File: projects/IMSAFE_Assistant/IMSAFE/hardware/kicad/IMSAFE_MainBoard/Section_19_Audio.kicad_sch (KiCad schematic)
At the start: 0 parts

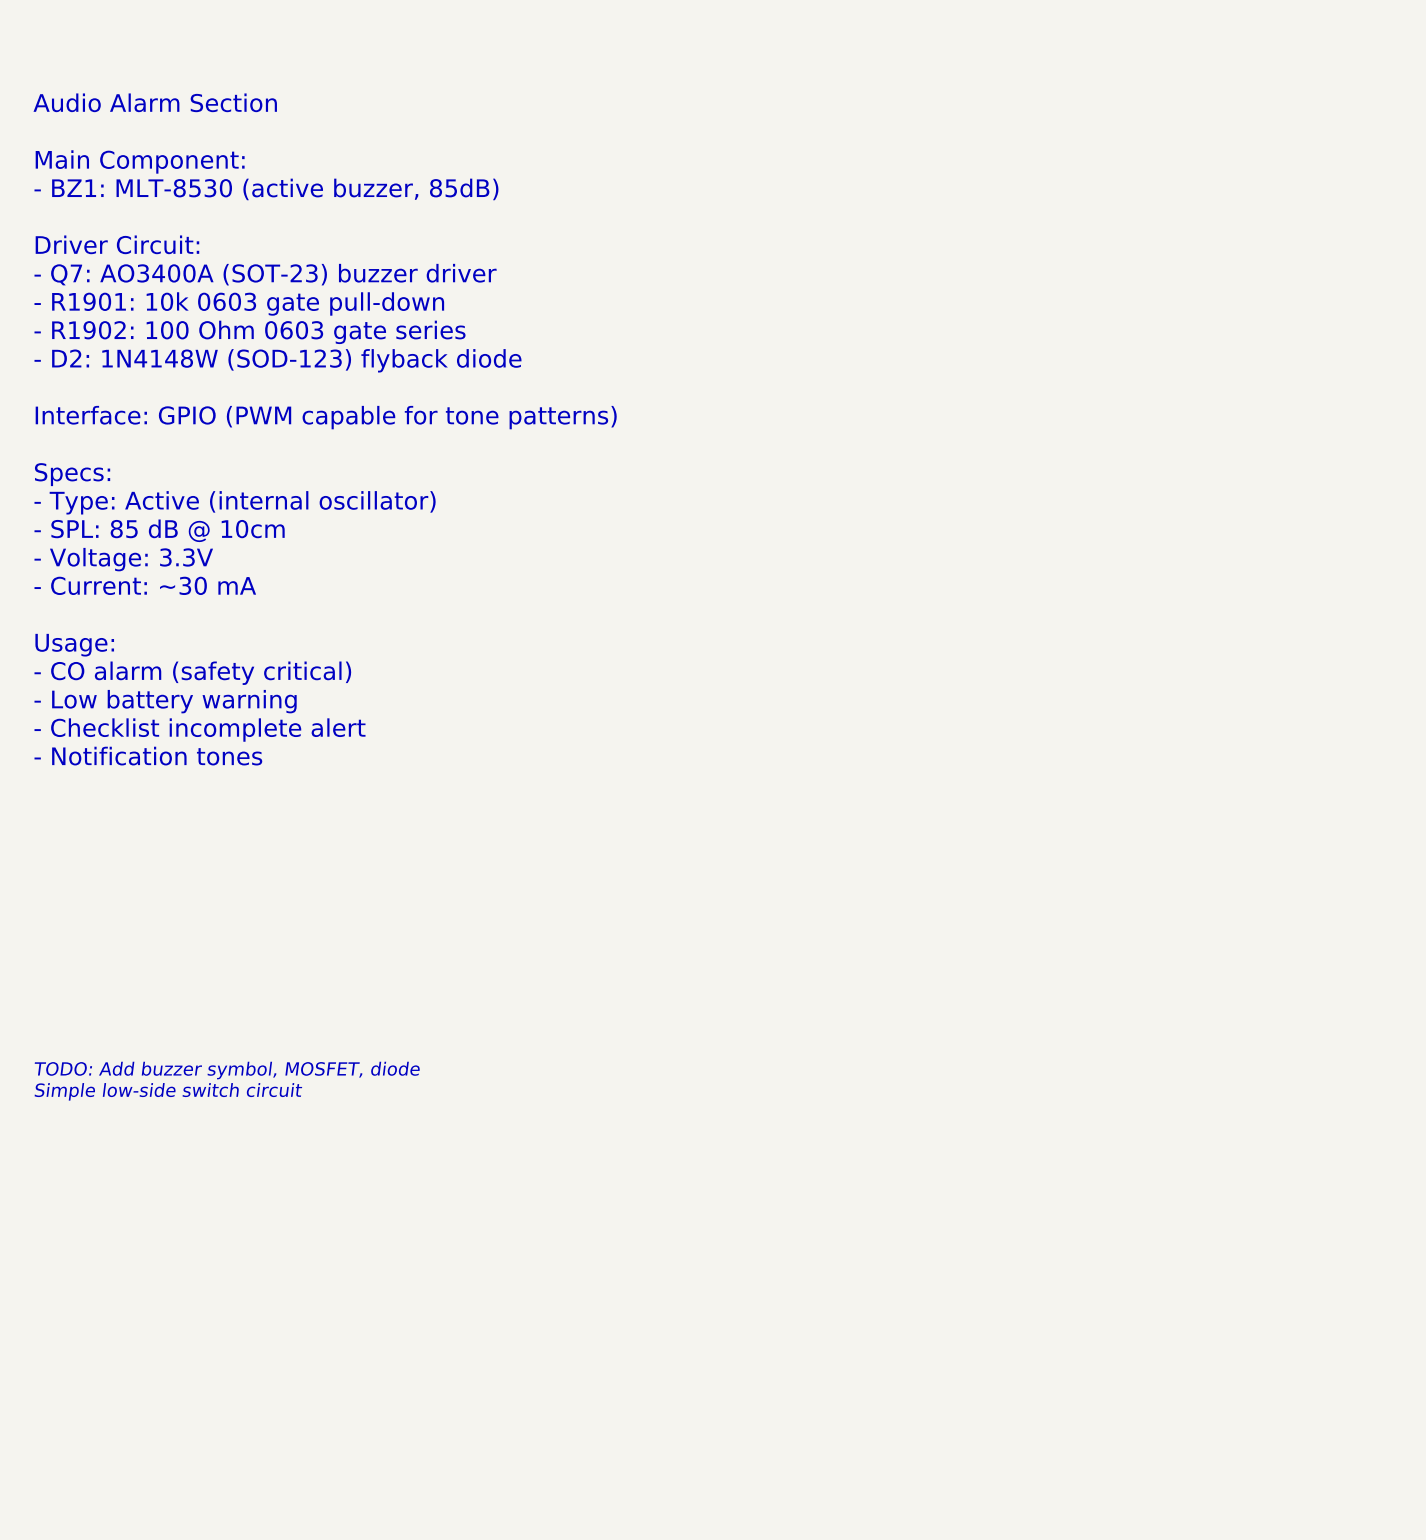
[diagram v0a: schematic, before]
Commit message: Add sensor and interface schematic implementations
- Section 01: MCU Core additional connections
- Section 04: BMS refinements
- Section 07: Barometric sensor (BMP390)
- Section 08: IMU (ICM-42688-P) full implementation
- Section 09: Magnetometer (MMC5983MA) full implementation
- Section 10: Gas sensor (MICS-4514) with heater control
- Section 11: Temp/Humidity (Si7021-A20) implementation
- Section 14: I/O Expander updates
- Section 16: Rotary encoder connections
- Section 19: Audio buzzer (MLT-8530) with MOSFET driver

Co-Authored-By: Claude Opus 4.5 <noreply@anthropic.com>
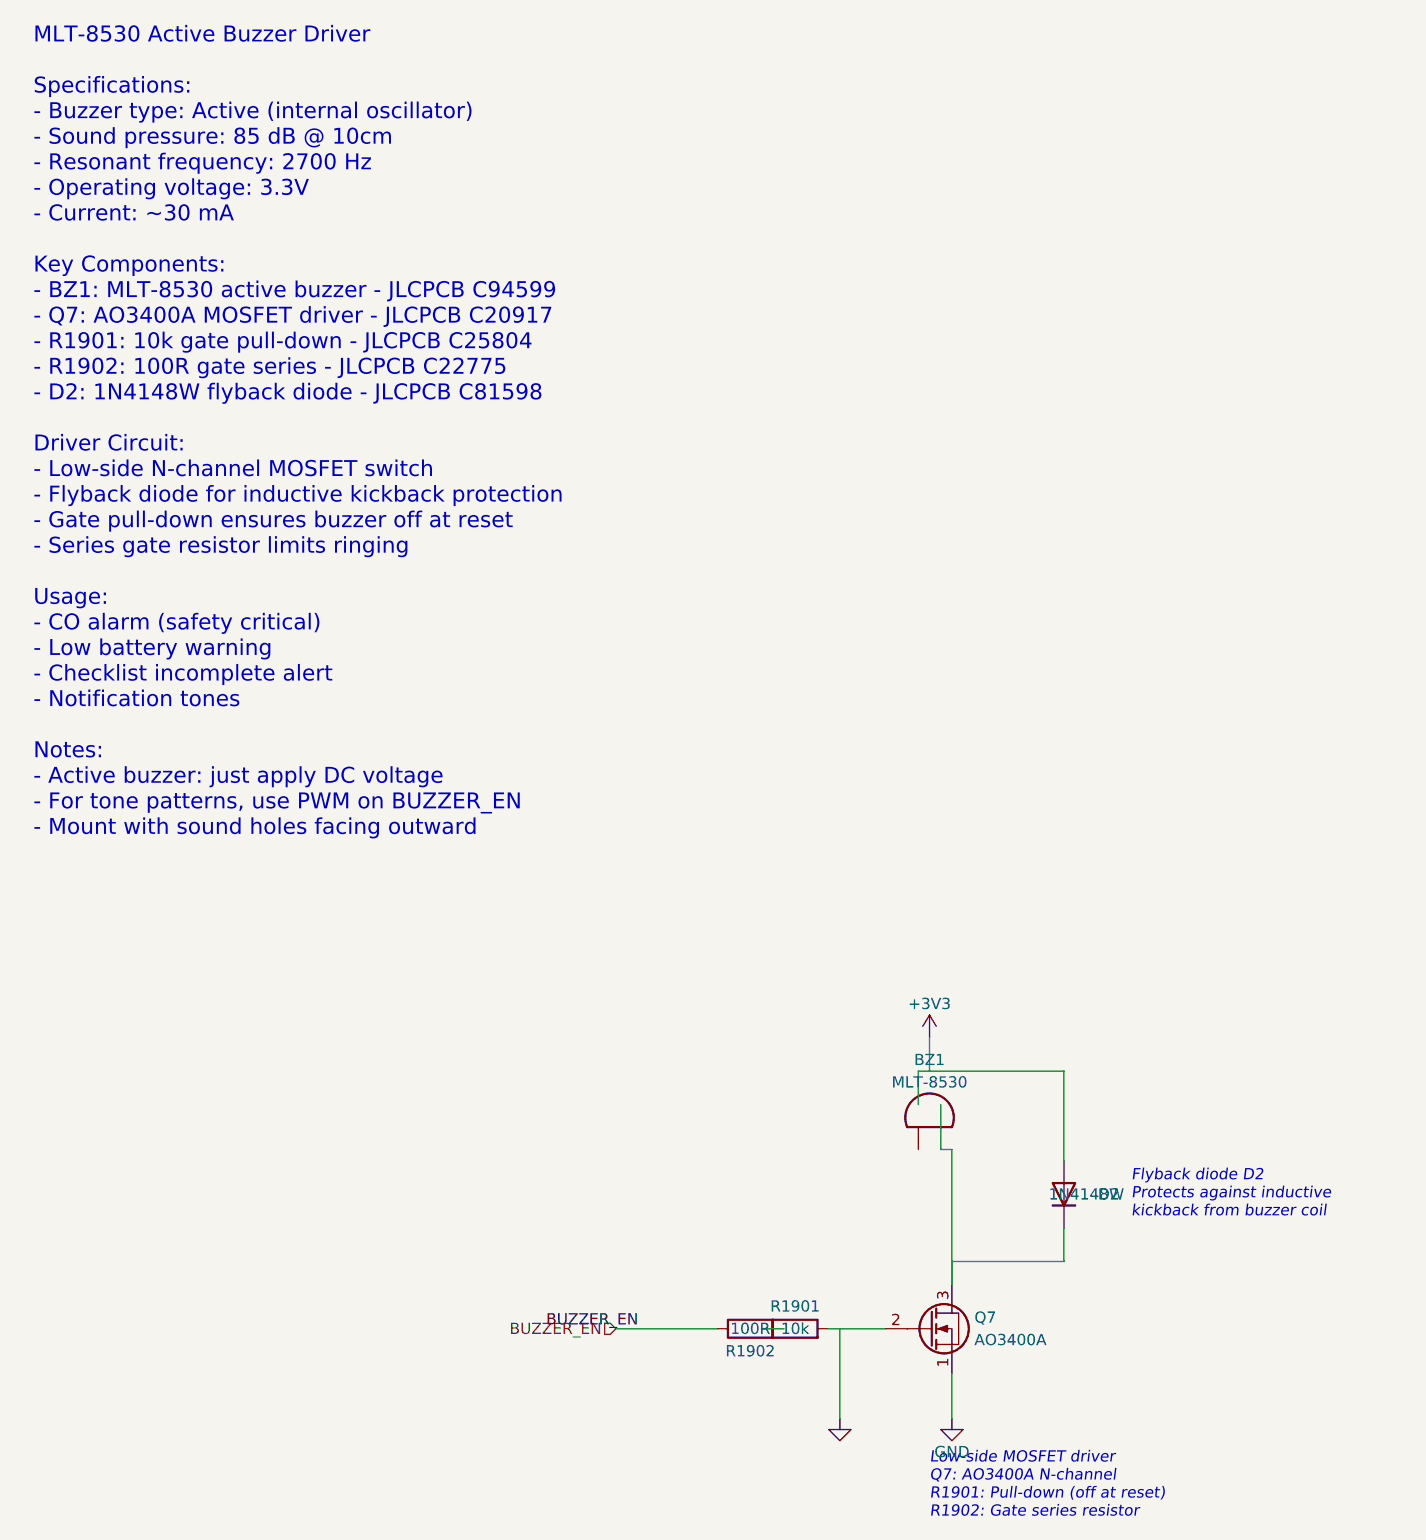
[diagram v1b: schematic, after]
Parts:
- added BZ1: MLT-8530, Buzzer_Beeper:Buzzer_12x9.5RM7.6, symbol Device:Buzzer
- added D2: 1N4148W, Diode_SMD:D_SOD-123, symbol Device:D
- added Q7: AO3400A, Package_TO_SOT_SMD:SOT-23, symbol Transistor_FET:AO3400A
- added R1901: 10k, Resistor_SMD:R_0603_1608Metric, symbol Device:R
- added R1902: 100R, Resistor_SMD:R_0603_1608Metric, symbol Device:R
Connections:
- new net: BZ1.2 (-), D2.1 (K), Q7.3 (D)
- new net: R1901.1, R1902.2
- new net +3V3: D2.2 (A)
- new net BUZZER_EN: R1902.1
- new net GND: Q7.1 (S), Q7.2 (G), R1901.2
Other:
- note added: "Flyback diode D2 Protects against inductive kickback from buzzer coil"
- note added: "Low-side MOSFET driver Q7: AO3400A N-channel R1901: Pull-down (off at reset) R1902: Gate series resistor"
- note added: "MLT-8530 Active Buzzer Driver Specifications: - Buzzer type: Active (internal oscillator) - Sound pressure: 85 dB @ 10cm - Resonant frequency: 2700 Hz - Operating voltage: 3.3V - Current: ~30 mA Key Components: - BZ1: MLT-8530 active buzzer - JLCPCB C94599 - Q7: AO3400A MOSFET driver - JLCPCB C20917 - R1901: 10k gate pull-down - JLCPCB C25804 - R1902: 100R gate series - JLCPCB C22775 - D2: 1N4148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"
- note removed: "Audio Alarm Section Main Component: - BZ1: MLT-8530 (active buzzer, 85dB) Driver Circuit: - Q7: AO3400A (SOT-23) buzzer driver - R1901: 10k 0603 gate pull-down - R1902: 100 Ohm 0603 gate series - D2: 1N4148W (SOD-123) flyback diode Interface: GPIO (PWM capable for tone patterns) Specs: - Type: Active (internal oscillator) - SPL: 85 dB @ 10cm - Voltage: 3.3V - Current: ~30 mA Usage: - CO alarm (sa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"
- note removed: "TODO: Add buzzer symbol, MOSFET, diode Simple low-side switch circuit"

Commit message: Update KiCad schematics and add analysis files
- Update all MainBoard schematic sections with component placement
- Add ERC reports and analysis scripts for schematic validation
- Update Radar Interface and SwitchLED Board projects
- Sync KiCad project files with latest session changes

Co-Authored-By: Claude Opus 4.5 <noreply@anthropic.com>
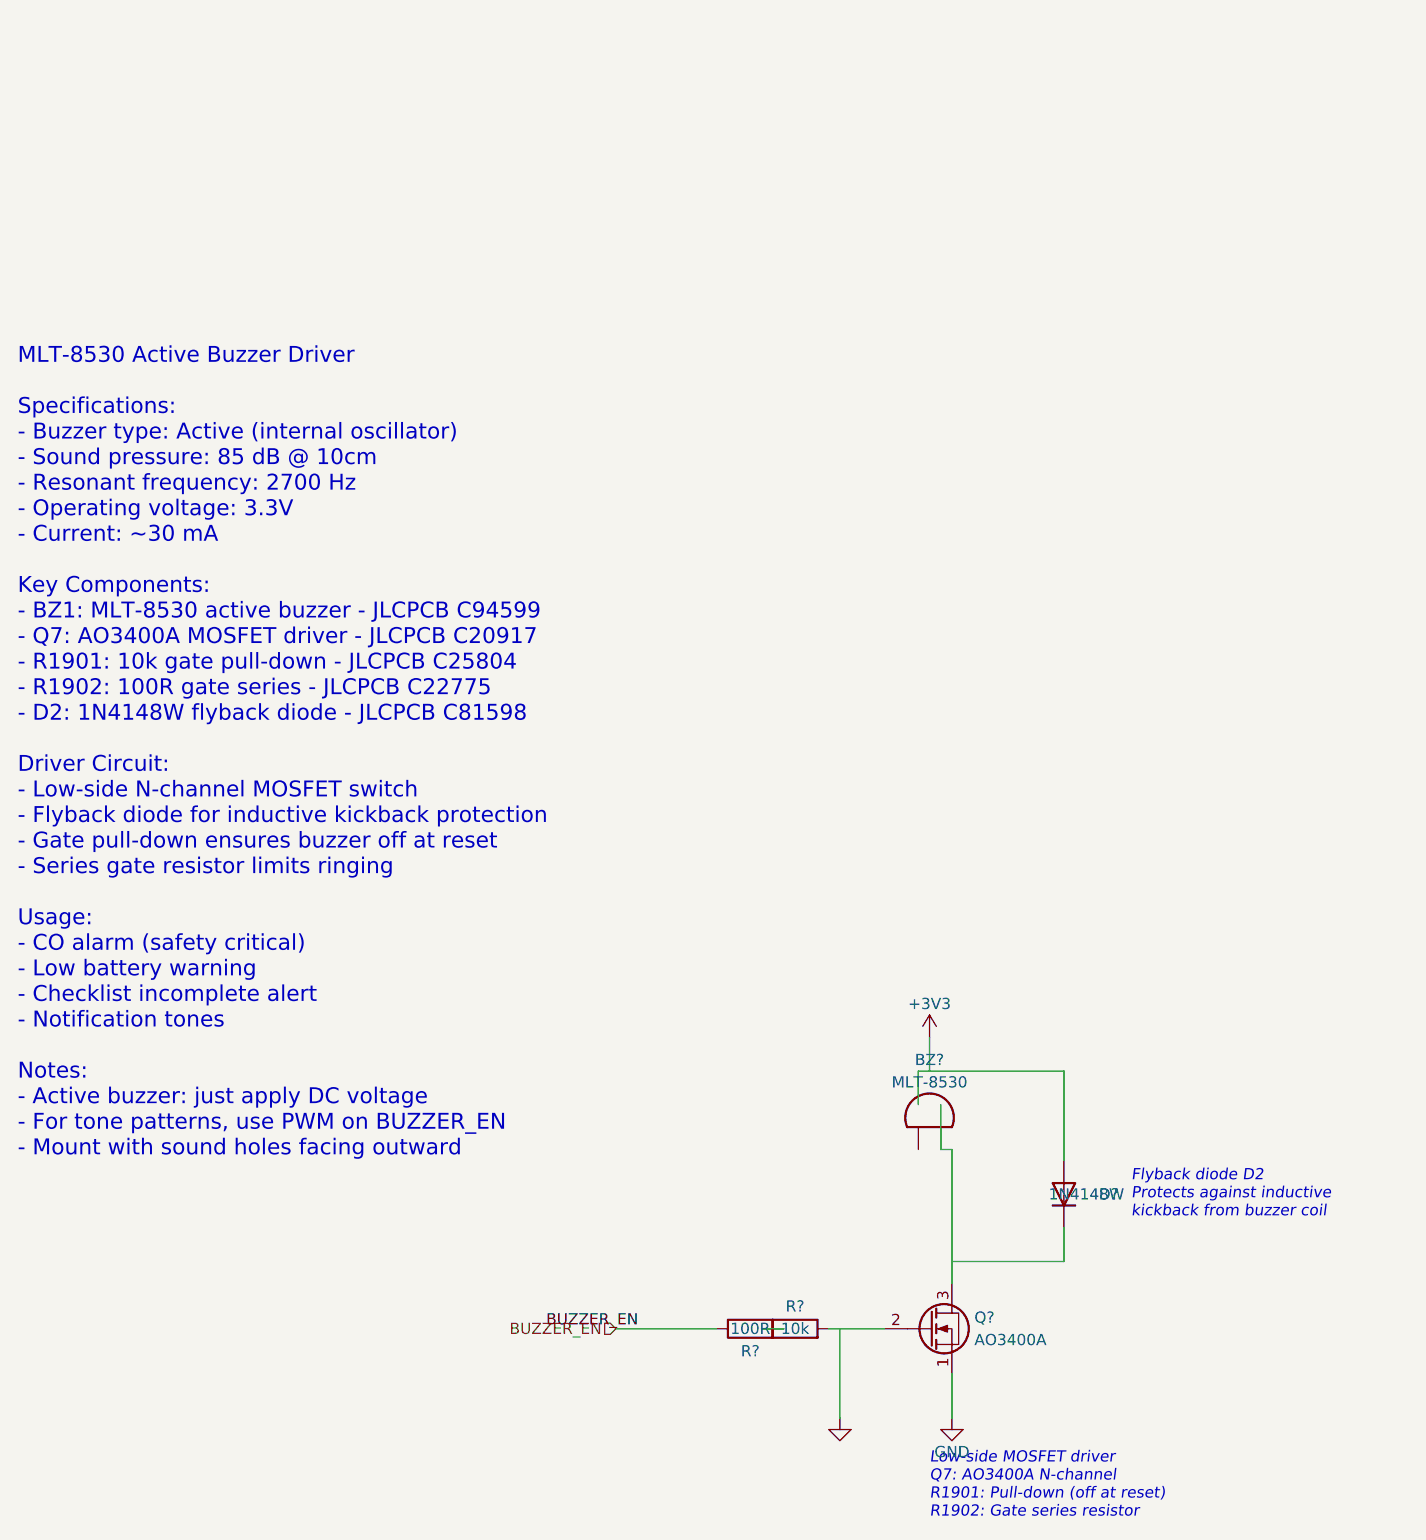
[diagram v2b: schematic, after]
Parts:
- removed BZ1: MLT-8530, Buzzer_Beeper:Buzzer_12x9.5RM7.6, symbol Device:Buzzer
- removed D2: 1N4148W, Diode_SMD:D_SOD-123, symbol Device:D
- removed Q7: AO3400A, Package_TO_SOT_SMD:SOT-23, symbol Transistor_FET:AO3400A
- removed R1901: 10k, Resistor_SMD:R_0603_1608Metric, symbol Device:R
- removed R1902: 100R, Resistor_SMD:R_0603_1608Metric, symbol Device:R
- added BZ?: MLT-8530, Buzzer_Beeper:Buzzer_12x9.5RM7.6, symbol Device:Buzzer
- added D?: 1N4148W, Diode_SMD:D_SOD-123, symbol Device:D
- added Q?: AO3400A, Package_TO_SOT_SMD:SOT-23, symbol Transistor_FET:AO3400A
- added R?: 10k, Resistor_SMD:R_0603_1608Metric, symbol Device:R
- added R?: 100R, Resistor_SMD:R_0603_1608Metric, symbol Device:R
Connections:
- net +3V3: now also D?.2 (A)
- net BUZZER_EN: now also R?.1
- net GND: now also Q?.1 (S), Q?.2 (G), R?.2
- new net: R?.1, R?.2
- new net: BZ?.2 (-), Q?.3 (D)
